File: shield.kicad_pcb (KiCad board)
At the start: 4 copper layers, 78.9 x 53.8 mm, 189 parts, among them J1 USB_C_Receptacle_USB2.0_14P, J10 BM03B-SRSS-TB, J2 USB_A, J3 USB_A, J4 BM03B-SRSS-TB, J5 BM03B-SRSS-TB, J6 BM03B-SRSS-TB, J7 Conn_ARM_JTAG_SWD_10, J9 BM03B-SRSS-TB, SW1 SW_Push, SW2 SW_Push, SW3 SW_Push, SW4 SW_Push, U10 SRV05-4, U11 SRV05-4, U12 RP2354B, U13 RP2354B, U15 AMS1117-3.3, U2 SRV05-4, U3 M24C02-WMN, U4 CH334F, U8 INA219AxDCN, U9 INA219AxDCN, Y1 12Mhz, Y2 ABM8-272-T3, Y3 ABM8-272-T3

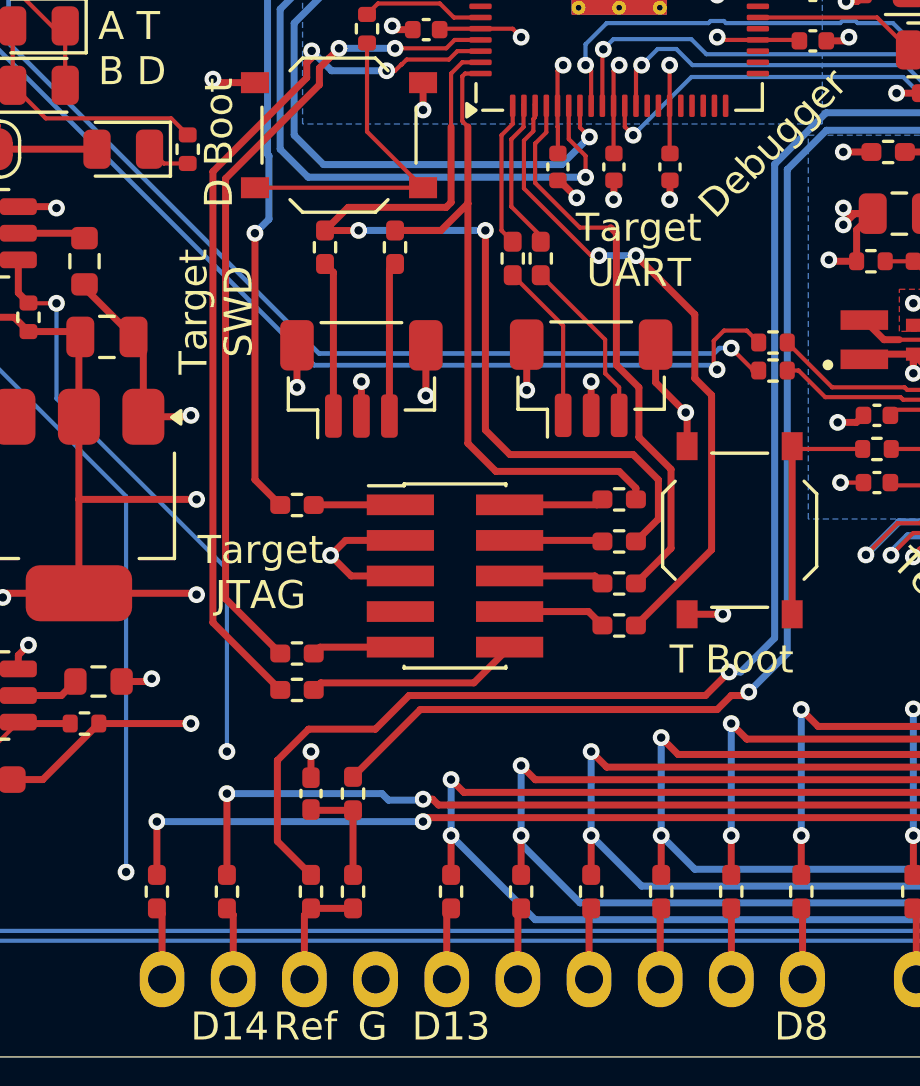
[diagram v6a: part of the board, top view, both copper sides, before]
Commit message: JLC rotations
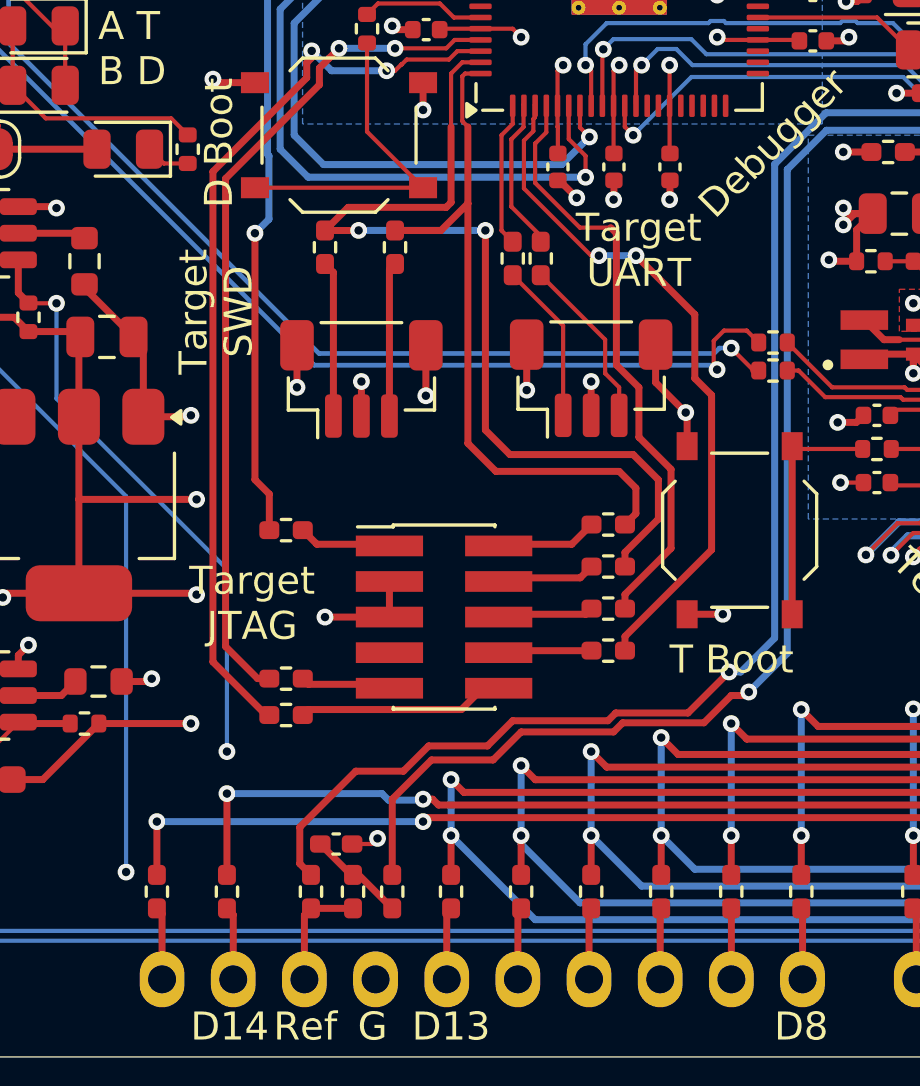
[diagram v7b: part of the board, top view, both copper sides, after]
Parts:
- U5, U6, U7: value ~ -> CH217K
- moved R52 3.77 mm to (68.9, 79.0)
- moved C11 2.01 mm to (66.9, 77.3), turned to 0 degrees
- moved J7 1.52 mm to (70.8, 69.2)
- moved R70 0.98 mm to (65.1, 72.7)
- moved R69 0.98 mm to (65.1, 66.1)
- moved R71 0.98 mm to (76.6, 67.4)
- moved R72 0.98 mm to (76.6, 65.9)
- moved R73 0.98 mm to (76.6, 68.9)
- moved R74 0.98 mm to (76.6, 70.4)
- moved R81 0.98 mm to (65.1, 71.4)
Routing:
- net /Tester/A6: track 57.5 -> 54.9 mm
- net GND: track 212.1 -> 210.2 mm
- net /Tester/PWM6: track 56.7 -> 58.4 mm
- net /debugger/SWO: track 20.4 -> 21.5 mm
- net /debugger/SWCLK: track 33.2 -> 34.3 mm
- net /debugger/TDI: track 23.6 -> 24.7 mm
- net /debugger/SWD: track 24.0 -> 25.0 mm
- net /debugger/GNDDetect: track 29.3 -> 30.3 mm
- net /debugger/~{TARGET_RESET}: track 31.9 -> 32.7 mm
- net /debugger/Vref: track 45.2 -> 46.0 mm

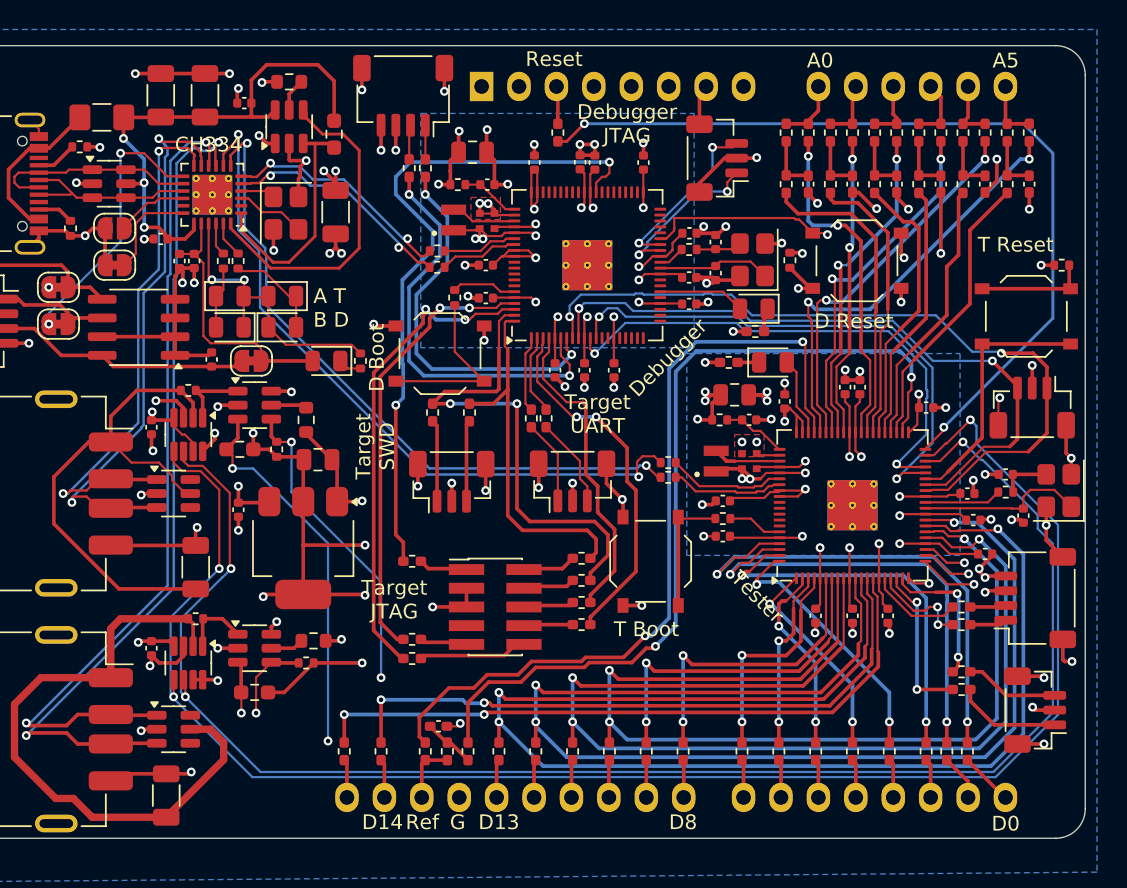
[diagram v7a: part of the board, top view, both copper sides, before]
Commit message: Fix JTAG IDC
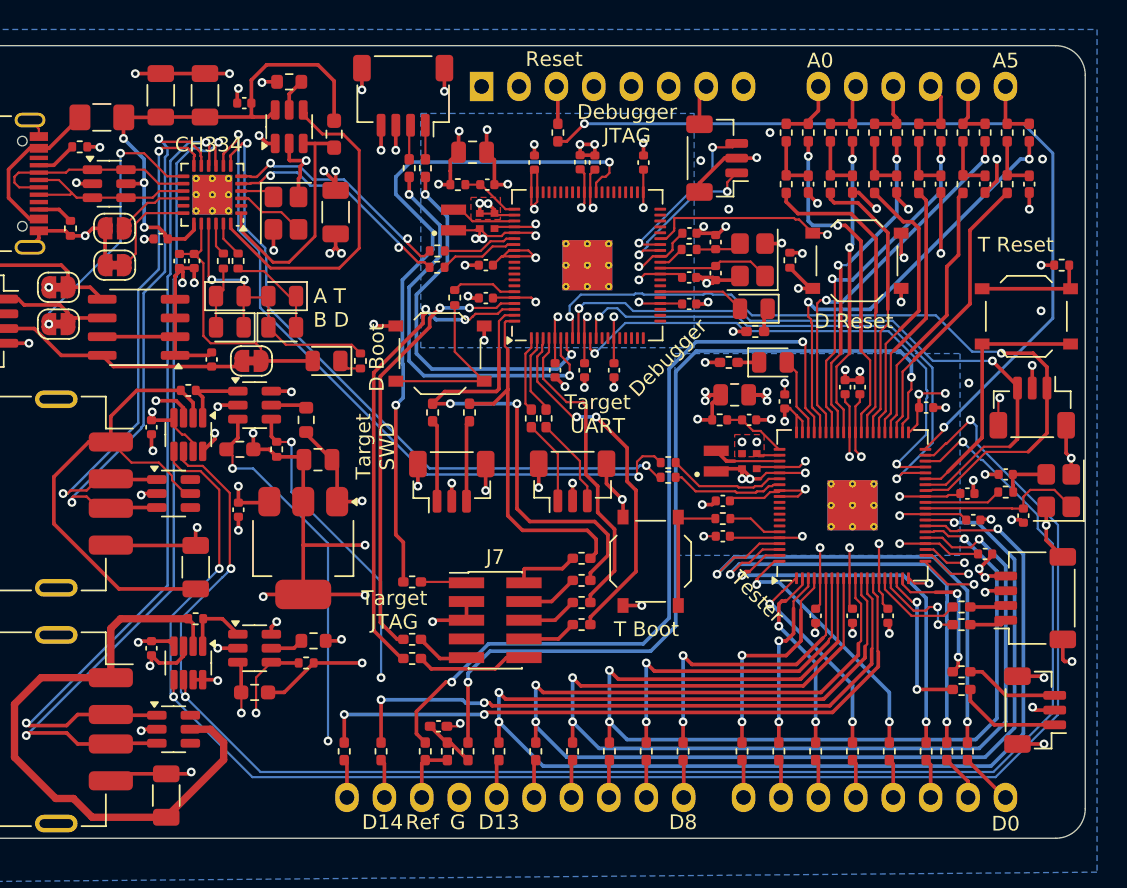
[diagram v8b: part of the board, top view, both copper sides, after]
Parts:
- J7: footprint Connector_PinHeader_1.27mm:PinHeader_2x05_P1.27mm_Vertical_SMD -> ProjectSpecific:PinHeader_2x05_P1.27mm_Vertical_SMD_IDC
- moved R69 1.40 mm to (65.1, 67.5)
- moved J7 0.90 mm to (70.8, 70.1)
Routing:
- net GND: track 210.2 -> 206.6 mm
- net /debugger/Vref: track 46.0 -> 47.4 mm
- net +3V3: track 153.4 -> 152.4 mm, vias 34 -> 41
- net /Tester/PWM6: track 58.4 -> 59.4 mm
- net /USB/USB1.D-: track 36.4 -> 35.5 mm
- net /USB/USB1.D+: track 38.2 -> 37.3 mm
- net Net-(J7-SWDIO/TMS): track 3.63 -> 4.53 mm
- net Net-(D3-K): track 6.90 -> 6.23 mm
- net /Tester/A6: track 54.9 -> 55.5 mm
- net Net-(C17-Pad1): track 3.11 -> 2.54 mm
- net Net-(U4-XI): track 2.35 -> 1.79 mm
- net /debugger/RP2350B1/VREG_LX: track 4.52 -> 4.02 mm
